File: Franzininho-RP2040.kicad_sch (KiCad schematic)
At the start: 41 parts, among them J1 USB_B_Micro, J3 Conn_01x04, J4 Conn_01x17, J5 Conn_01x17, SW1 SW_Push, SW2 SW_Push, U1 RP2040, U2 XC6206P332MR, U3 W25Q128JVS, Y1 12MHz

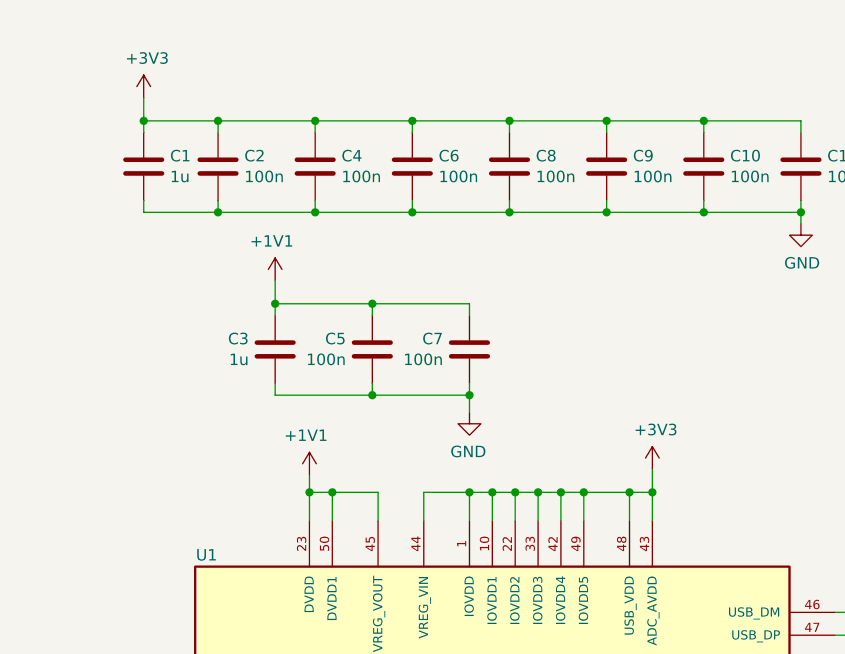
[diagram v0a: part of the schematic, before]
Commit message: Adição de título
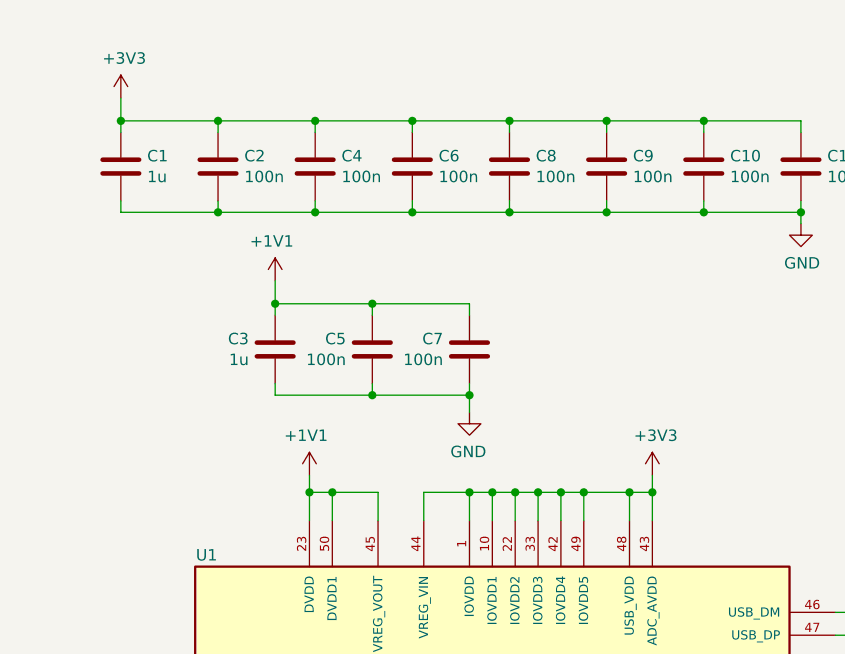
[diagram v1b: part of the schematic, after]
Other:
- company: (none) -> Projeto Franzininho
- title: (none) -> Franzininho RP2040
- moved on the sheet: C1
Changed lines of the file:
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@@
 (kicad_sch (version 20211123) (generator eeschema)
   (paper "A4")
+  (title_block
+    (title "Franzininho RP2040")
+    (date "2022-01-30")
+    (rev "0.1")
+    (company "Projeto Franzininho")
+  )
   (junction (at 73.025 23.495) (diameter 0) (color 0 0 0 0)
   )
+  (junction (at 29.845 23.495) (diameter 0) (color 0 0 0 0)
+  )
   (junction (at 105.41 33.655) (diameter 0) (color 0 0 0 0)
   )
   (junction (at 170.18 38.1) (diameter 0) (color 0 0 0 0)
-  )
-  (junction (at 32.385 23.495) (diameter 0) (color 0 0 0 0)
   )
   (junction (at 40.64 33.655) (diameter 0) (color 0 0 0 0)
@@
     (stroke (width 0) (type default) (color 0 0 0 0))
   )
-  (wire (pts (xy 88.9 62.23) (xy 88.9 64.77))
+  (wire (pts (xy 88.9 62.865) (xy 88.9 64.77))
     (stroke (width 0) (type default) (color 0 0 0 0))
   )
@@
     (stroke (width 0) (type default) (color 0 0 0 0))
   )
-  (wire (pts (xy 32.385 20.955) (xy 32.385 23.495))
+  (wire (pts (xy 29.845 20.955) (xy 29.845 23.495))
     (stroke (width 0) (type default) (color 0 0 0 0))
   )
@@
     (stroke (width 0) (type default) (color 0 0 0 0))
   )
-  (wire (pts (xy 32.385 32.385) (xy 32.385 33.655))
+  (wire (pts (xy 29.845 32.385) (xy 29.845 33.655))
     (stroke (width 0) (type default) (color 0 0 0 0))
   )
@@
     (stroke (width 0) (type default) (color 0 0 0 0))
   )
-  (wire (pts (xy 40.64 33.655) (xy 32.385 33.655))
+  (wire (pts (xy 40.64 33.655) (xy 29.845 33.655))
     (stroke (width 0) (type default) (color 0 0 0 0))
   )
@@
     (stroke (width 0) (type default) (color 0 0 0 0))
   )
-  (wire (pts (xy 32.385 23.495) (xy 32.385 24.765))
+  (wire (pts (xy 29.845 23.495) (xy 29.845 24.765))
     (stroke (width 0) (type default) (color 0 0 0 0))
   )
@@
     (stroke (width 0) (type default) (color 0 0 0 0))
   )
-  (wire (pts (xy 32.385 23.495) (xy 40.64 23.495))
+  (wire (pts (xy 29.845 23.495) (xy 40.64 23.495))
     (stroke (width 0) (type default) (color 0 0 0 0))
   )
@@
     (pin "1")
   )
-  (symbol (lib_id "power:+3V3") (at 32.385 20.955 0) (unit 1)
-    (in_bom yes) (on_board yes)
-    (property "Reference" "#PWR01" (id 0) (at 32.385 24.765 0)
-      (effects (font (size 1.27 1.27)) hide)
-    )
-    (property "Value" "+3V3" (id 1) (at 32.766 16.5608 0))
-    (property "Footprint" "" (id 2) (at 32.385 20.955 0)
-      (effects (font (size 1.27 1.27)) hide)
-    )
-    (property "Datasheet" "" (id 3) (at 32.385 20.955 0)
-      (effects (font (size 1.27 1.27)) hide)
-    )
-    (pin "1")
-  )
-  (symbol (lib_id "Device:C") (at 32.385 28.575 0) (unit 1)
-    (in_bom yes) (on_board yes)
-    (property "Reference" "C1" (id 0) (at 35.306 27.4066 0)
-      (effects (font (size 1.27 1.27)) (justify left))
-    )
-    (property "Value" "1u" (id 1) (at 35.306 29.718 0)
-      (effects (font (size 1.27 1.27)) (justify left))
-    )
-    (property "Footprint" "Capacitor_SMD:C_0402_1005Metric_Pad0.74x0.62mm_HandSolder" (id 2) (at 33.3502 32.385 0)
-      (effects (font (size 1.27 1.27)) hide)
-    )
-    (property "Datasheet" "~" (id 3) (at 32.385 28.575 0)
+  (symbol (lib_id "power:+3V3") (at 29.845 20.955 0) (unit 1)
+    (in_bom yes) (on_board yes)
+    (property "Reference" "#PWR01" (id 0) (at 29.845 24.765 0)
+      (effects (font (size 1.27 1.27)) hide)
+    )
+    (property "Value" "+3V3" (id 1) (at 30.226 16.5608 0))
+    (property "Footprint" "" (id 2) (at 29.845 20.955 0)
+      (effects (font (size 1.27 1.27)) hide)
+    )
+    (property "Datasheet" "" (id 3) (at 29.845 20.955 0)
+      (effects (font (size 1.27 1.27)) hide)
+    )
+    (pin "1")
+  )
+  (symbol (lib_id "Device:C") (at 29.845 28.575 0) (unit 1)
+    (in_bom yes) (on_board yes)
+    (property "Reference" "C1" (id 0) (at 32.766 27.4066 0)
+      (effects (font (size 1.27 1.27)) (justify left))
+    )
+    (property "Value" "1u" (id 1) (at 32.766 29.718 0)
+      (effects (font (size 1.27 1.27)) (justify left))
+    )
+    (property "Footprint" "Capacitor_SMD:C_0402_1005Metric_Pad0.74x0.62mm_HandSolder" (id 2) (at 30.8102 32.385 0)
+      (effects (font (size 1.27 1.27)) hide)
+    )
+    (property "Datasheet" "~" (id 3) (at 29.845 28.575 0)
       (effects (font (size 1.27 1.27)) hide)
     )
@@
     (pin "1")
   )
-  (symbol (lib_id "power:+3V3") (at 88.9 62.23 0) (unit 1)
-    (in_bom yes) (on_board yes)
-    (property "Reference" "#PWR07" (id 0) (at 88.9 66.04 0)
-      (effects (font (size 1.27 1.27)) hide)
-    )
-    (property "Value" "+3V3" (id 1) (at 89.281 57.8358 0))
-    (property "Footprint" "" (id 2) (at 88.9 62.23 0)
-      (effects (font (size 1.27 1.27)) hide)
-    )
-    (property "Datasheet" "" (id 3) (at 88.9 62.23 0)
-      (effects (font (size 1.27 1.27)) hide)
-    )
+  (symbol (lib_id "power:+3V3") (at 88.9 62.865 0) (unit 1)
+    (in_bom yes) (on_board yes)
+    (property "Reference" "#PWR07" (id 0) (at 88.9 66.675 0)
+      (effects (font (size 1.27 1.27)) hide)
+    )
+    (property "Value" "+3V3" (id 1) (at 89.281 58.4708 0))
+    (property "Footprint" "" (id 2) (at 88.9 62.865 0)
+      (effects (font (size 1.27 1.27)) hide)
+    )
+    (property "Datasheet" "" (id 3) (at 88.9 62.865 0)
+      (effects (font (size 1.27 1.27)) hide)
+    )

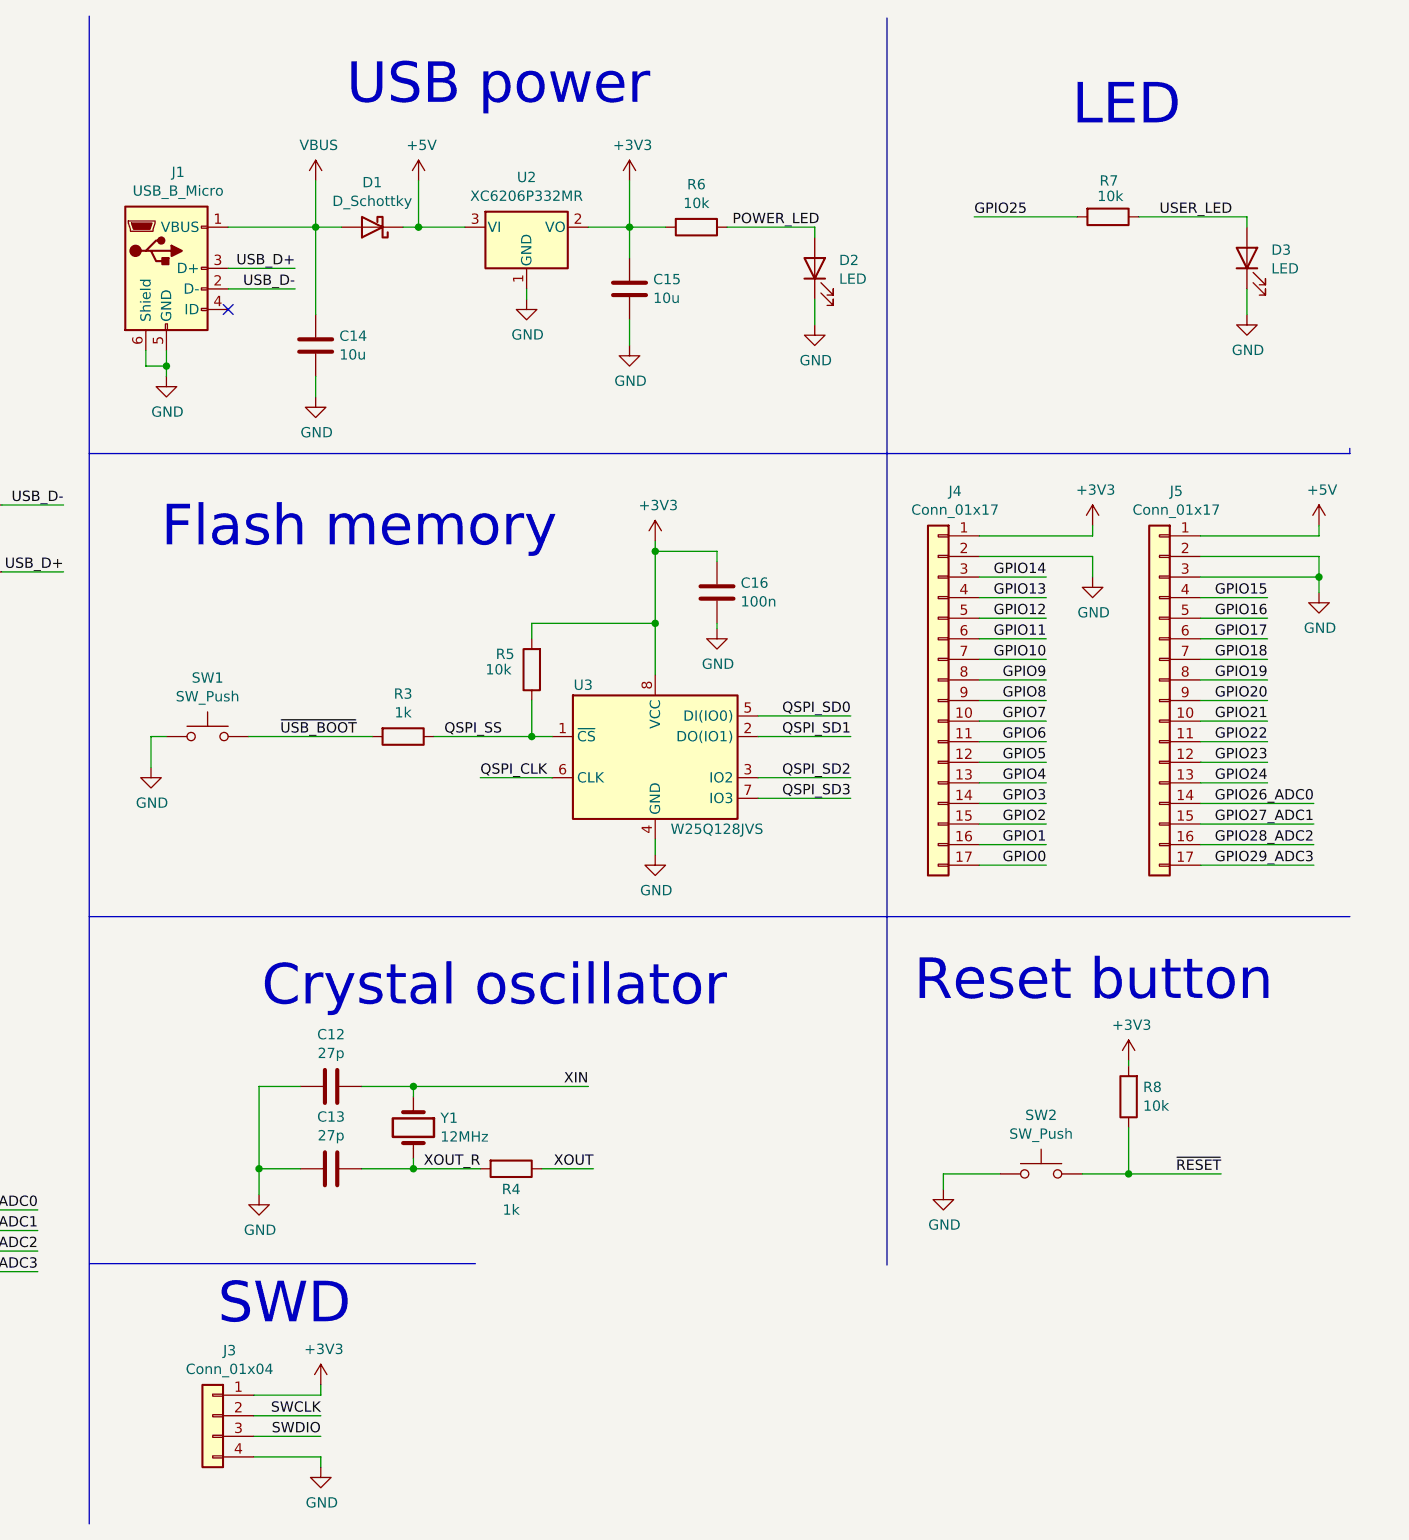
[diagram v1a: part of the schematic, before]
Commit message: Pequena melhoria nos textos do esquemático
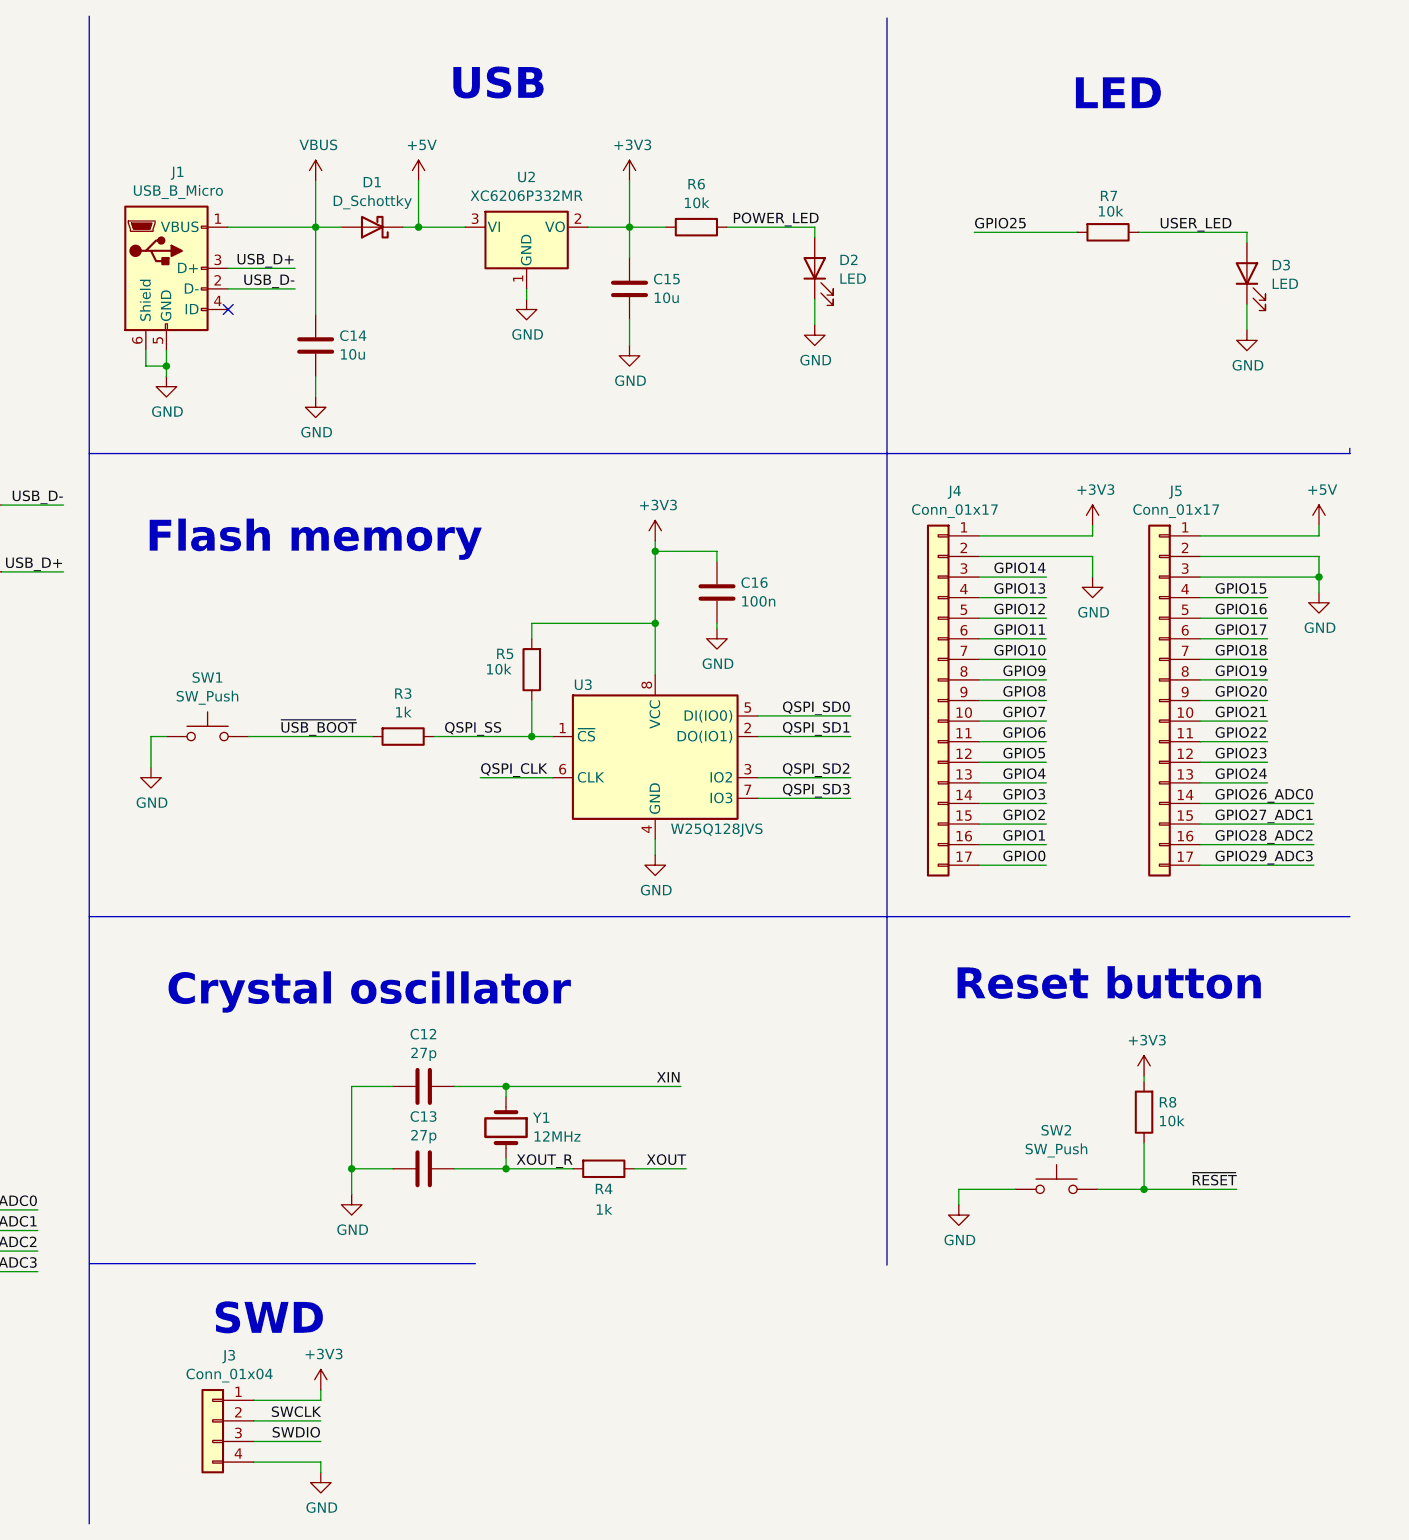
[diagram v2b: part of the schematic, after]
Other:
- note added: "USB"
- note removed: "USB power"
- moved on the sheet: C12, C13, D3, J3, R4, R7, R8, SW2, Y1
